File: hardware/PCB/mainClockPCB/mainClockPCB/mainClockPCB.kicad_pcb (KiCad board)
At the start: 2 copper layers, 48 parts, among them IC1 ESP32-S3-WROOM-1-N16R2, IC2 SPX1117M3-L_TR, IC3 MCP7940N-I_P, IC4 PAM8904QJER, J1 USB_C_Receptacle_USB2.0_16P, J2 Conn_01x09_Socket, J3 Conn_01x02_Socket, SW1 SW_Push, SW2 SW_Push, SW3 SW_Push, SW4 SW_Push, U1 PEC11R-4320K-S0012, U2 USBLC6-2SC6, Y1 AB26T-32.768KHZ-6

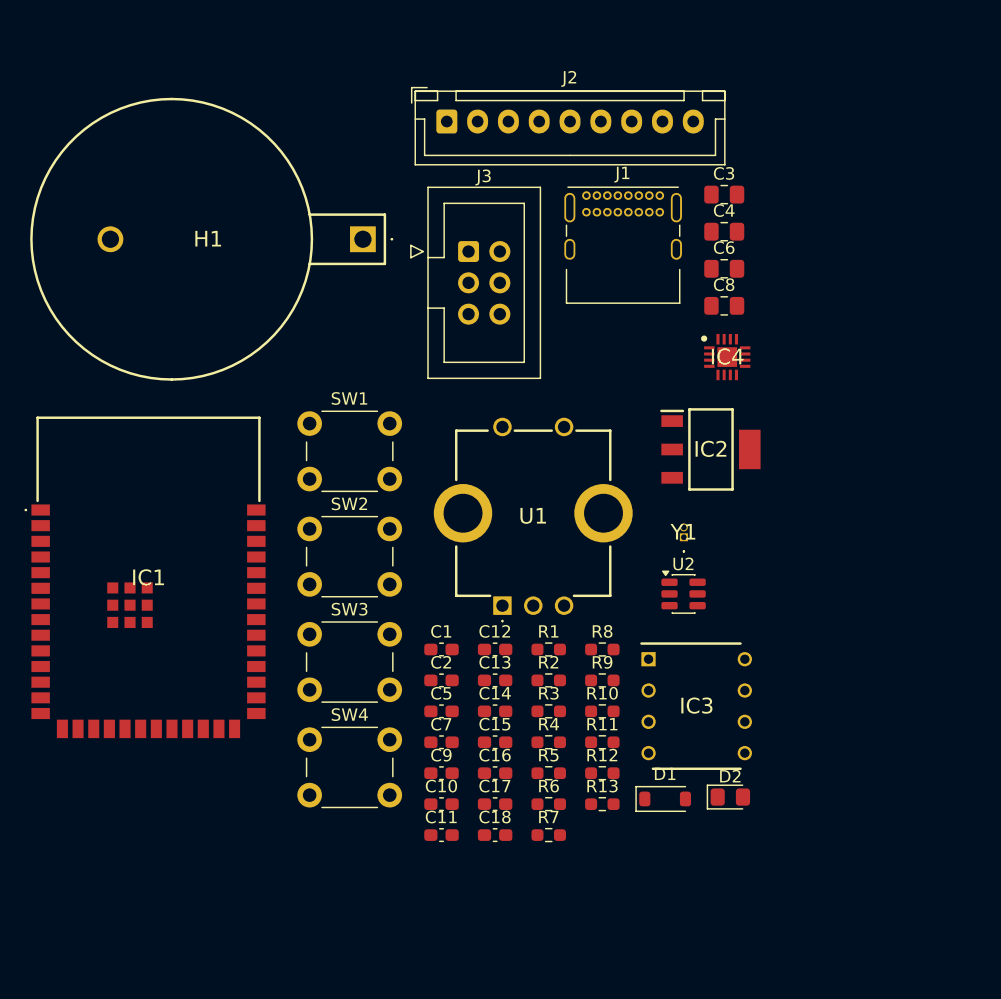
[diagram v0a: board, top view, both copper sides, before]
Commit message: net label fixes
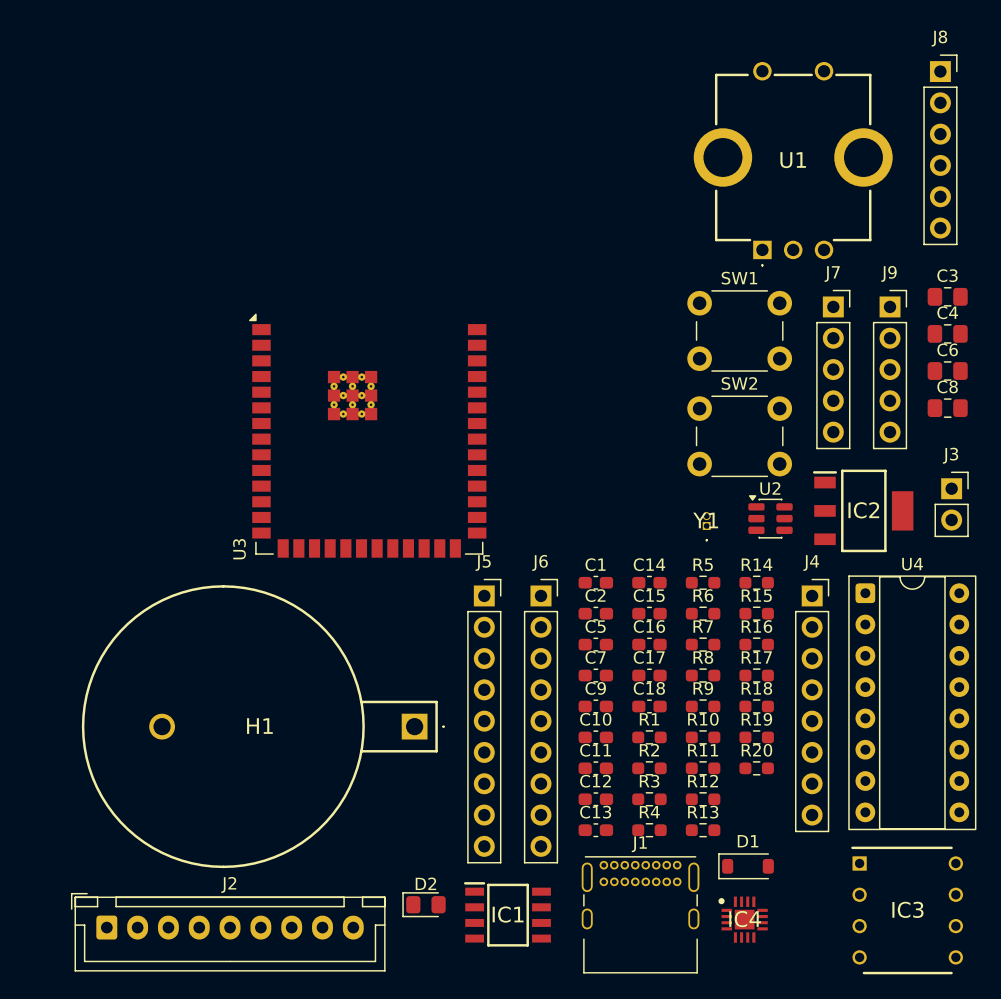
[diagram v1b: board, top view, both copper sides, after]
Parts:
- removed SW3, SW4: SW_Push, Button_Switch_THT:SW_PUSH_6mm_H5mm
- added J4: Conn_01x08, Connector_PinSocket_2.54mm:PinSocket_1x08_P2.54mm_Vertical, F.Cu at (152.9, 80.6)
- added J5: Conn_01x09, Connector_PinSocket_2.54mm:PinSocket_1x09_P2.54mm_Vertical, F.Cu at (126.3, 80.6)
- added J6: Conn_01x09, Connector_PinSocket_2.54mm:PinSocket_1x09_P2.54mm_Vertical, F.Cu at (130.9, 80.6)
- added J7: Conn_01x05, Connector_PinSocket_2.54mm:PinSocket_1x05_P2.54mm_Vertical, F.Cu at (154.7, 57.2)
- added J8: Conn_01x06, Connector_PinSocket_2.54mm:PinSocket_1x06_P2.54mm_Vertical, F.Cu at (163.4, 38.1)
- added J9: Conn_01x05, Connector_PinSocket_2.54mm:PinSocket_1x05_P2.54mm_Vertical, F.Cu at (159.3, 57.2)
- added R14: 10k, Resistor_SMD:R_0603_1608Metric_Pad0.98x0.95mm_HandSolder, F.Cu at (148.4, 79.5)
- added R15: 10k, Resistor_SMD:R_0603_1608Metric_Pad0.98x0.95mm_HandSolder, F.Cu at (148.4, 82.1)
- added R16: 10k, Resistor_SMD:R_0603_1608Metric_Pad0.98x0.95mm_HandSolder, F.Cu at (148.4, 84.6)
- added R17: 10k, Resistor_SMD:R_0603_1608Metric_Pad0.98x0.95mm_HandSolder, F.Cu at (148.4, 87.1)
- added R18: 10k, Resistor_SMD:R_0603_1608Metric_Pad0.98x0.95mm_HandSolder, F.Cu at (148.4, 89.6)
- added R19: 10k, Resistor_SMD:R_0603_1608Metric_Pad0.98x0.95mm_HandSolder, F.Cu at (148.4, 92.1)
- added R20: 10k, Resistor_SMD:R_0603_1608Metric_Pad0.98x0.95mm_HandSolder, F.Cu at (148.4, 94.6)
- added U3: ESP32-S3-WROOM-2, RF_Module:ESP32-S3-WROOM-2, F.Cu at (117.0, 64.3)
- added U4: 74HC165, Package_DIP:DIP-16_W7.62mm_Socket, F.Cu at (157.3, 80.4)
- C16: value 1uF -> 2.2uF
- C17, C18: value .1uF -> 1uF
- IC1: value ESP32-S3-WROOM-1-N16R2 -> TMP275AIDR; footprint SamacSys_Parts:ESP32S3WROOM1N16R2 -> SamacSys_Parts:SOIC127P600X175-8N
- J3: footprint Connector_IDC:IDC-Header_2x03_P2.54mm_Vertical -> Connector_PinSocket_2.54mm:PinSocket_1x02_P2.54mm_Vertical
- moved J2 71.0 mm to (95.7, 107.5)
- moved J1 54.4 mm to (136.0, 102.5)
- moved IC4 45.7 mm to (147.5, 106.9)
- moved J3 43.7 mm to (164.3, 71.9)
- moved IC1 40.2 mm to (128.3, 106.5)
- moved H1 39.8 mm to (120.7, 91.2)
- moved U1 35.8 mm to (148.9, 52.5)
- moved SW1 33.1 mm to (143.8, 56.9)
- moved SW2 33.1 mm to (143.8, 65.4)
- moved D2 26.2 mm to (121.6, 105.7)
- moved IC3 23.8 mm to (160.7, 106.1)
- moved C3 19.9 mm to (163.9, 56.4)
- moved C4 19.9 mm to (163.9, 59.4)
- moved C6 19.9 mm to (163.9, 62.4)
- moved C8 19.9 mm to (163.9, 65.4)
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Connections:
- net Net-(D1-A) renamed /VBUS
- net Net-(H1-+) renamed /RTC_BAT
- net Net-(IC4-CN1) renamed /CN1
- net Net-(IC4-VO2) renamed /PIEZO_VO2
- net Net-(J1-CC1) renamed /CC1
- net Net-(J1-CC2) renamed /CC2
- net Net-(J1-D+-PadA6) renamed /D+
- net Net-(J1-D--PadA7) renamed /D-
- C1 pad 1: /ENABLE -> ENABLE
- C1 pad 2: /PIN_ENCODER_PUSH -> GND
- C10 pad 1: /ENABLE -> ENABLE
- C10 pad 2: /PIN_ENCODER_PUSH -> GND
- C11 pad 1: /PIN_ENCODER_B -> ENCODER_B
- C11 pad 2: /PIN_ENCODER_PUSH -> GND
- C12 pad 1: /PIN_ENCODER_A -> GND
- C12 pad 2: /PIN_ENCODER_PUSH -> ENCODER_A
- C13 pad 1: Net-(IC1-IO0) -> GPIO0
- C13 pad 2: /PIN_ENCODER_PUSH -> GND
- C14 pad 1: Net-(IC3-X2) -> GND
- C14 pad 2: /PIN_ENCODER_PUSH -> /X2
- C15 pad 1: Net-(IC3-X1) -> GND
- C15 pad 2: /PIN_ENCODER_PUSH -> /X1
- C16 pad 1: /PIN_ENCODER_PUSH -> /PZ_VOUT
- C16 pad 2: Net-(IC4-VOUT) -> GND
- C17 pad 1: Net-(IC4-CP2) -> /CN2
- C17 pad 2: Net-(IC4-CN2) -> /CP2
- C18 pad 2: Net-(IC4-CN2) -> /CP1
- C2 pad 1: /PIN_ENCODER_PUSH -> ENCODER_PUSH
- C2 pad 2: /PIN_ENCODER_PUSH -> ESP_3v3
- C3 pad 1: /PIN_ENCODER_PUSH -> GND
- C3 pad 2: /PIN_ENCODER_PUSH -> VCC_5V
- C4 pad 1: /PIN_ENCODER_PUSH -> +5V
- C4 pad 2: /PIN_ENCODER_PUSH -> GND
- C5 pad 1: /PIN_ENCODER_PUSH -> +5V
- C5 pad 2: /PIN_ENCODER_PUSH -> GND
- C6 pad 2: /PIN_ENCODER_PUSH -> GND
- C7 pad 2: /PIN_ENCODER_PUSH -> GND
- C8 pad 2: /PIN_ENCODER_PUSH -> GND
- C9 pad 2: /PIN_ENCODER_PUSH -> GND
- D1 pad 1: /PIN_ENCODER_PUSH -> VCC_5V
- D2 pad 1: /PIN_ENCODER_PUSH -> GND
- H1 pad 2: /PIN_ENCODER_PUSH -> GND
- IC1 pad 1: /PIN_ENCODER_PUSH -> SDA
- IC1 pad 2: /ESP_3V3 -> SCL
- IC1 pad 3: /ENABLE -> unconnected-(IC1-ALERT-Pad3)
- IC1 pad 4: Net-(IC1-IO13) -> GND
- IC1 pad 5: Net-(IC1-IO5) -> GND
- IC1 pad 6: Net-(IC1-IO6) -> GND
- IC1 pad 7: Net-(IC1-IO7) -> GND
- IC1 pad 8: unconnected-(IC1-IO15-Pad8) -> ESP_3v3
- IC2 pad 1: /PIN_ENCODER_PUSH -> GND
- IC2 pad 3: /PIN_ENCODER_PUSH -> +5V
- IC3 pad 1: Net-(IC3-X1) -> /X1
- IC3 pad 2: Net-(IC3-X2) -> /X2
- IC3 pad 4: /PIN_ENCODER_PUSH -> GND
- IC3 pad 5: Net-(IC1-IO38) -> SDA
- IC3 pad 6: Net-(IC1-IO39) -> SCL
- IC3 pad 7: Net-(IC1-IO41) -> MFP
- IC3 pad 8: /ESP_3V3 -> ESP_3v3
- IC4 pad 1: /PIN_ENCODER_PUSH -> +5V
- IC4 pad 10: Net-(IC4-CN2) -> /CN2
- IC4 pad 11: Net-(IC4-CN2) -> /CP1
- IC4 pad 13: Net-(IC4-VOUT) -> /PZ_VOUT
- IC4 pad 14: Net-(IC4-CP2) -> /CP2
- IC4 pad 15: /PIN_ENCODER_PUSH -> +5V
- IC4 pad 17: /PIN_ENCODER_PUSH -> GND
- IC4 pad 2: /PIN_ENCODER_PUSH -> +5V
- IC4 pad 3: /PIN_ENCODER_PUSH -> PIN_DIN
- IC4 pad 6: /PIN_ENCODER_PUSH -> GND
- IC4 pad 9: Net-(IC4-CN2) -> /PIEZO_VO1
- J1 pad A1: /PIN_ENCODER_PUSH -> GND
- J1 pad A12: /PIN_ENCODER_PUSH -> GND
- J1 pad B1: /PIN_ENCODER_PUSH -> GND
- J1 pad B12: /PIN_ENCODER_PUSH -> GND
- J1 pad S1: /PIN_ENCODER_PUSH -> GND
- J2 pad 1: Net-(IC1-IO13) -> OE_PWM
- J2 pad 2: Net-(IC1-IO13) -> SERIAL
- J2 pad 3: Net-(IC1-IO12) -> SRCLK
- J2 pad 4: Net-(IC1-IO40) -> RCLK
- J2 pad 5: /ESP_3V3 -> ESP_3v3
- J2 pad 6: /PIN_ENCODER_PUSH -> GND
- J2 pad 7: /PIN_ENCODER_PUSH -> +5V
- J2 pad 8: /PIN_ENCODER_PUSH -> GND
- J2 pad 9: Net-(IC1-IO7) -> LIGHT_SENSOR
- J3 pad 1: Net-(IC4-CN2) -> /PIEZO_VO1
- R1 pad 2: /PIN_ENCODER_PUSH -> GND
- R10 pad 1: /ESP_3V3 -> /A_CHANNEL
- R10 pad 2: Net-(U1-CHANNEL_A) -> ESP_3v3
- R11 pad 1: /ESP_3V3 -> /B_CHANNEL
- R11 pad 2: Net-(U1-CHANNEL_B) -> ESP_3v3
- R12 pad 1: /ESP_3V3 -> ESP_3v3
- R12 pad 2: Net-(IC1-IO38) -> SDA
- R13 pad 1: /ESP_3V3 -> ESP_3v3
- R13 pad 2: Net-(IC1-IO39) -> SCL
- R2 pad 2: /PIN_ENCODER_PUSH -> GND
- R3 pad 1: Net-(D2-A) -> /VCC_3V3
- R3 pad 2: /VCC_3V3 -> Net-(D2-A)
- R4 pad 1: /ESP_3V3 -> /VCC_3V3
- R4 pad 2: /VCC_3V3 -> ESP_3v3
- R5 pad 1: /ESP_3V3 -> ENABLE
- R5 pad 2: /ENABLE -> ESP_3v3
- R6 pad 1: /ESP_3V3 -> GND
- R6 pad 2: Net-(IC1-IO0) -> GPIO0
- R7 pad 1: /PIN_ENCODER_B -> ENCODER_B
- R7 pad 2: Net-(U1-CHANNEL_B) -> /B_CHANNEL
- R8 pad 1: /PIN_ENCODER_A -> ENCODER_A
- R8 pad 2: Net-(U1-CHANNEL_A) -> /A_CHANNEL
- R9 pad 1: /ESP_3V3 -> ESP_3v3
- R9 pad 2: /PIN_ENCODER_PUSH -> ENCODER_PUSH
- SW1 pad 1: /PIN_ENCODER_PUSH -> GND
- SW1 pad 2: Net-(IC1-IO0) -> GPIO0
- SW2 pad 1: /ENABLE -> GND
- SW2 pad 2: /PIN_ENCODER_PUSH -> ENABLE
- U1 pad 1: /PIN_ENCODER_PUSH -> GND
- U1 pad 2: /PIN_ENCODER_PUSH -> ENCODER_PUSH
- U1 pad 3: /PIN_ENCODER_PUSH -> GND
- U1 pad 4: /PIN_ENCODER_PUSH -> GND
- U1 pad A1: Net-(U1-CHANNEL_A) -> /A_CHANNEL
- U1 pad B1: Net-(U1-CHANNEL_B) -> /B_CHANNEL
- U1 pad C1: /PIN_ENCODER_PUSH -> GND
- U2 pad 2: /PIN_ENCODER_PUSH -> GND
- U2 pad 4: Net-(IC1-IO20) -> USB_D+
- U2 pad 6: Net-(IC1-IO19) -> USB_D-
- Y1 pad 1: Net-(IC3-X1) -> /X1
- Y1 pad 2: Net-(IC3-X2) -> /X2

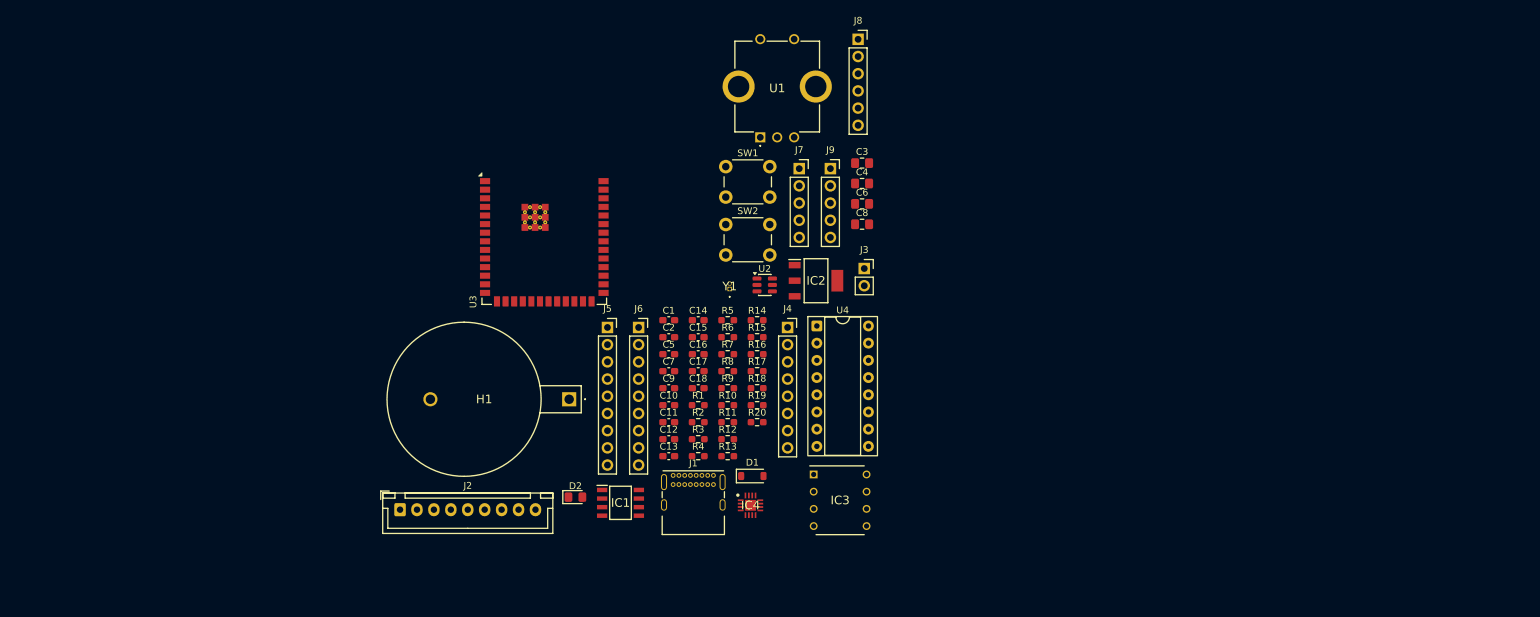
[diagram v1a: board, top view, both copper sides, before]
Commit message: begin PCB design. Component layout early draft, fills, edge cuts, board setup
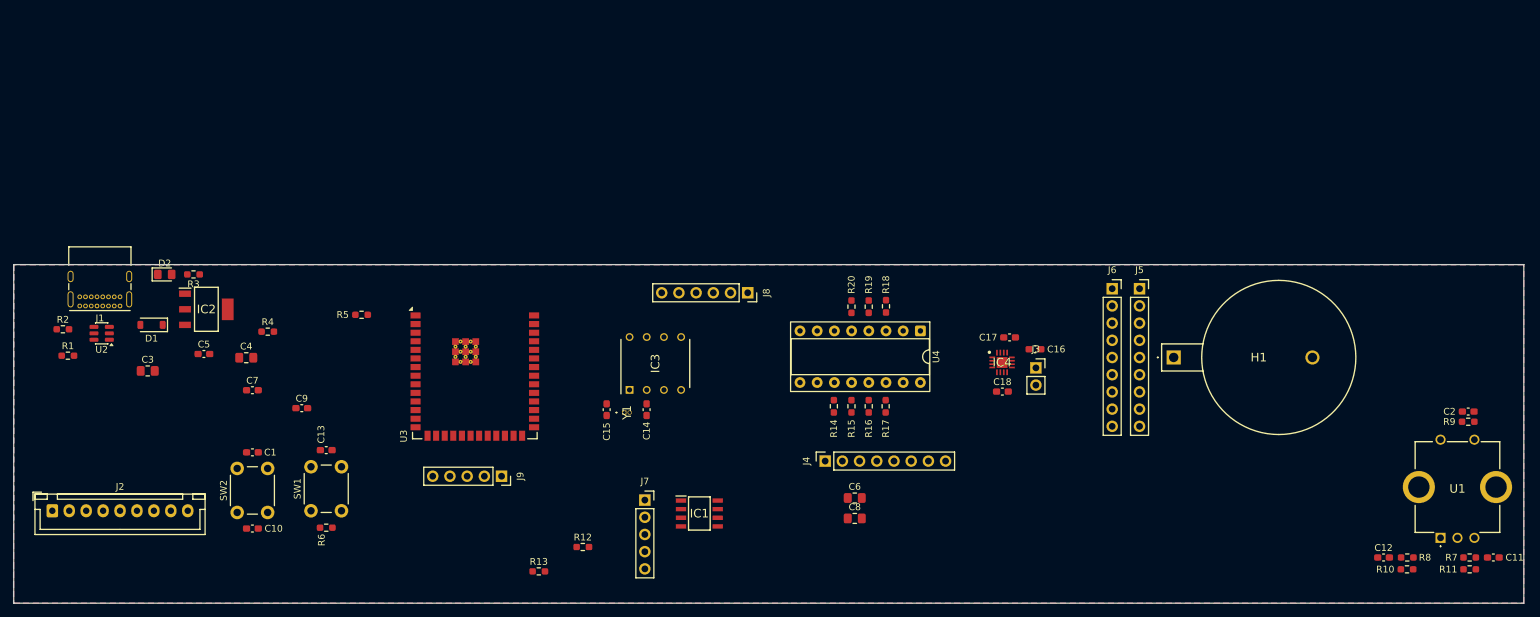
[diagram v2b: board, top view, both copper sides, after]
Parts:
- moved C11 123.4 mm to (257.2, 114.6)
- moved C2 118.6 mm to (253.5, 93.0), turned to 180 degrees
- moved U1 116.6 mm to (249.4, 111.7)
- moved R7 113.6 mm to (253.7, 114.6), turned to 180 degrees
- moved R11 111.7 mm to (253.7, 116.3)
- moved C3 109.9 mm to (58.5, 87.0)
- moved R9 109.5 mm to (253.5, 94.5)
- moved C12 107.0 mm to (241.0, 114.6)
- moved R8 104.1 mm to (244.5, 114.6)
- moved R10 103.2 mm to (244.4, 116.3), turned to 180 degrees
- moved U2 98.2 mm to (51.7, 81.5), turned to 180 degrees
- moved R2 94.8 mm to (45.9, 80.9)
- moved C4 94.5 mm to (73.0, 85.1)
- moved R1 93.4 mm to (46.7, 84.8)
- moved D1 91.5 mm to (59.0, 80.2), turned to 180 degrees
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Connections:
- C3 pad 2: VCC_5V -> +5V
- D1 pad 1: VCC_5V -> +5V
- J6 pad 1: GPIO2 -> unconnected-(J6-Pin_1-Pad1)
- U3 pad 38: GPIO2 -> PIN_DIN
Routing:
- added copper zone on In1.Cu, net +5V
- added copper zone on In1.Cu, net ESP_3v3
- added copper zone on B.Cu, net GND
- added copper zone on F.Cu, net GND
- added copper zone on In2.Cu, net GND
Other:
- board outline added: 223 x 50 mm
- copper layers 2 -> 4

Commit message: PCB design complete
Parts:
- added REF**: MountingHole_3.2mm_M3_Pad_Via, MountingHole:MountingHole_3.2mm_M3_Pad_Via, F.Cu at (42.5, 76.2)
- added REF**: MountingHole_3.2mm_M3_Pad_Via, MountingHole:MountingHole_3.2mm_M3_Pad_Via, F.Cu at (45.0, 114.8)
- added REF**: MountingHole_3.2mm_M3_Pad_Via, MountingHole:MountingHole_3.2mm_M3_Pad_Via, F.Cu at (64.6, 99.8)
- added REF**: MountingHole_3.2mm_M3_Pad_Via, MountingHole:MountingHole_3.2mm_M3_Pad_Via, F.Cu at (255.3, 77.3)
- added REF**: MountingHole_3.2mm_M3_Pad_Via, MountingHole:MountingHole_3.2mm_M3_Pad_Via, F.Cu at (177.3, 84.2)
- added REF**: MountingHole_3.2mm_M3_Pad_Via, MountingHole:MountingHole_3.2mm_M3_Pad_Via, F.Cu at (240.5, 90.7)
- added REF**: MountingHole_3.2mm_M3_Pad_Via, MountingHole:MountingHole_3.2mm_M3_Pad_Via, F.Cu at (119.6, 108.3)
- J3: footprint Connector_PinSocket_2.54mm:PinSocket_1x02_P2.54mm_Vertical -> Connector_JST:JST_XH_B2B-XH-A_1x02_P2.50mm_Vertical
- J4: footprint Connector_PinSocket_2.54mm:PinSocket_1x08_P2.54mm_Vertical -> Connector_JST:JST_XH_B8B-XH-A_1x08_P2.50mm_Vertical
- moved C8 98.0 mm to (70.9, 75.1)
- moved C6 97.8 mm to (67.6, 83.6), turned to -90 degrees
- moved J4 76.3 mm to (230.8, 76.1), turned to 180 degrees
- moved H1 68.2 mm to (142.3, 93.4)
- moved R14 66.3 mm to (225.8, 85.5)
- moved R15 60.7 mm to (222.7, 85.5)
- moved J3 57.0 mm to (246.6, 84.2)
- moved R16 55.2 mm to (219.7, 85.5)
- moved C16 54.7 mm to (243.9, 78.8)
- moved C17 54.7 mm to (240.2, 77.0)
- moved C18 54.7 mm to (239.1, 85.0)
- moved IC4 54.7 mm to (239.1, 80.7)
- moved R17 49.7 mm to (216.6, 85.5)
- moved R13 48.4 mm to (146.1, 78.6), turned to 180 degrees
- moved IC1 47.8 mm to (92.2, 104.0)
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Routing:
- net +5V: track 0.00 -> 227.3 mm, vias 0 -> 10
- net ENCODER_PUSH: track 0.00 -> 190.8 mm, vias 0 -> 2
- net ENCODER_B: track 0.00 -> 166.8 mm, vias 0 -> 2
- net ENCODER_A: track 0.00 -> 153.6 mm
- net SDA: track 0.00 -> 142.9 mm, vias 0 -> 4
- net SCL: track 0.00 -> 140.0 mm, vias 0 -> 5
- net PIN_DIN: track 0.00 -> 123.1 mm, vias 0 -> 2
- net BUTTON_SRCLK: track 0.00 -> 119.3 mm, vias 0 -> 4
- net BUTTON_RCLK: track 0.00 -> 94.9 mm, vias 0 -> 2
- net BUTTON_SERIAL: track 0.00 -> 93.7 mm, vias 0 -> 3
- net GPIO16: track 0.00 -> 91.2 mm, vias 0 -> 2
- net GPIO17: track 0.00 -> 90.2 mm, vias 0 -> 2
- net GPIO18: track 0.00 -> 89.9 mm, vias 0 -> 2
- net GPIO47: track 0.00 -> 82.7 mm
- net GPIO21: track 0.00 -> 78.5 mm
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- added copper zone on In2.Cu, net +5V
- added copper zone on In2.Cu, net ESP_3v3
- added copper zone on In1.Cu, net GND
- removed copper zone on In1.Cu, net +5V
- removed copper zone on In1.Cu, net ESP_3v3
- removed copper zone on In2.Cu, net GND
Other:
- board text added: "2026-02-26"
- board text added: "3v3"
- board text added: "5v"
- board text added: "A"
- board text added: "ANALOG"
- board text added: "B"
- board text added: "C"
- board text added: "CINCINNATI, OHIO"
- board text added: "CR2032"
- board text added: "D"
- board text added: "DEBUG"
- board text added: "DISPLAY HEADER"
- board text added: "DISPLAY PINOUT INTENDED FOR: 12C-LTP-587HR REV D"
- board text added: "E"
- board text added: "ESP32-MB-EX"
- board text added: "EXPANSION BAY"
- board text added: "GND"
- board text added: "GPIO16"
- board text added: "GPIO17"
- board text added: "GPIO18"
- board text added: "GPIO21"
- board text added: "GPIO47"
- board text added: "GPIO48"
- board text added: "HEADERS 50mm APART"
- board text added: "HOME"
- board text added: "IC1"
- board text added: "J1"
- board text added: "JTAG ONLY"
- board text added: "KiCAD 9.0"
- board text added: "MOD"
- board text added: "MTCK"
- board text added: "MTDI"
- board text added: "MTDO"
- board text added: "MTMS"
- board text added: "NATHANIEL KESSEL"
- board text added: "NC"
- board text added: "OE_PWM"
- board text added: "RCLK"
- board text added: "REV A"
- board text added: "RTC BATTERY"
- board text added: "RX"
- board text added: "SCL"
- board text added: "SDA"
- board text added: "SER"
- board text added: "SRCLK"
- board text added: "ST3"
- board text added: "ST45"
- board text added: "ST46"
- board text added: "STRAPPING ONLY"
- board text added: "TX"

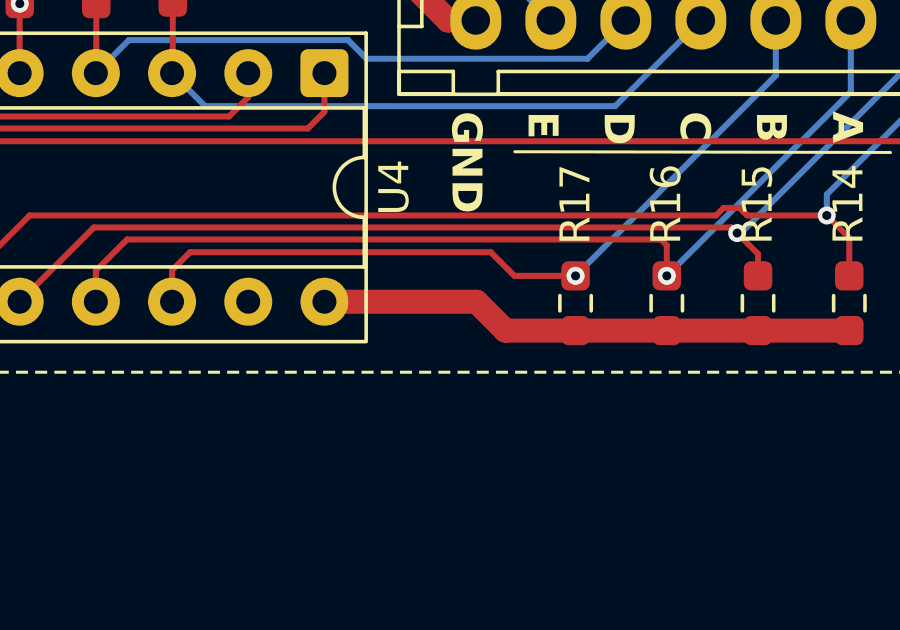
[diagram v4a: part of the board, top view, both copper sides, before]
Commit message: bypass cap on PISO S
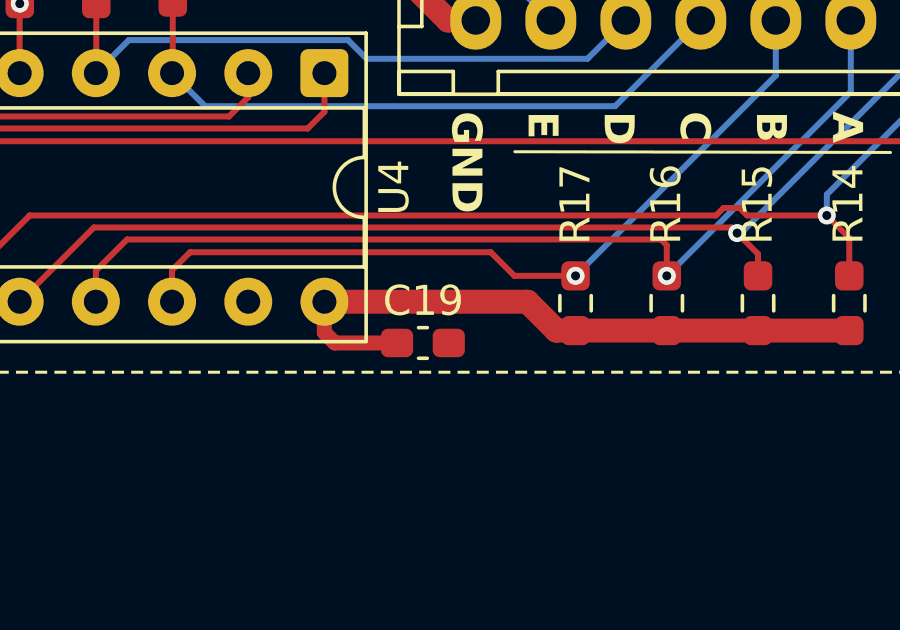
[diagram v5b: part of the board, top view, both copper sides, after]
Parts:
- added C19: 0.1uF, Capacitor_SMD:C_0603_1608Metric_Pad1.08x0.95mm_HandSolder, F.Cu at (211.5, 86.8)
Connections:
- U4 pad 15: unconnected-(U4-~{CE}-Pad15) -> GND
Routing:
- net ESP_3v3: track 44.3 -> 47.9 mm
